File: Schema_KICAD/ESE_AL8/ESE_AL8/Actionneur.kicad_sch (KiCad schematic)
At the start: 15 parts, among them J1 ECRAN, U2 ZXBM5210-SP, U3 ZXBM5210-SP

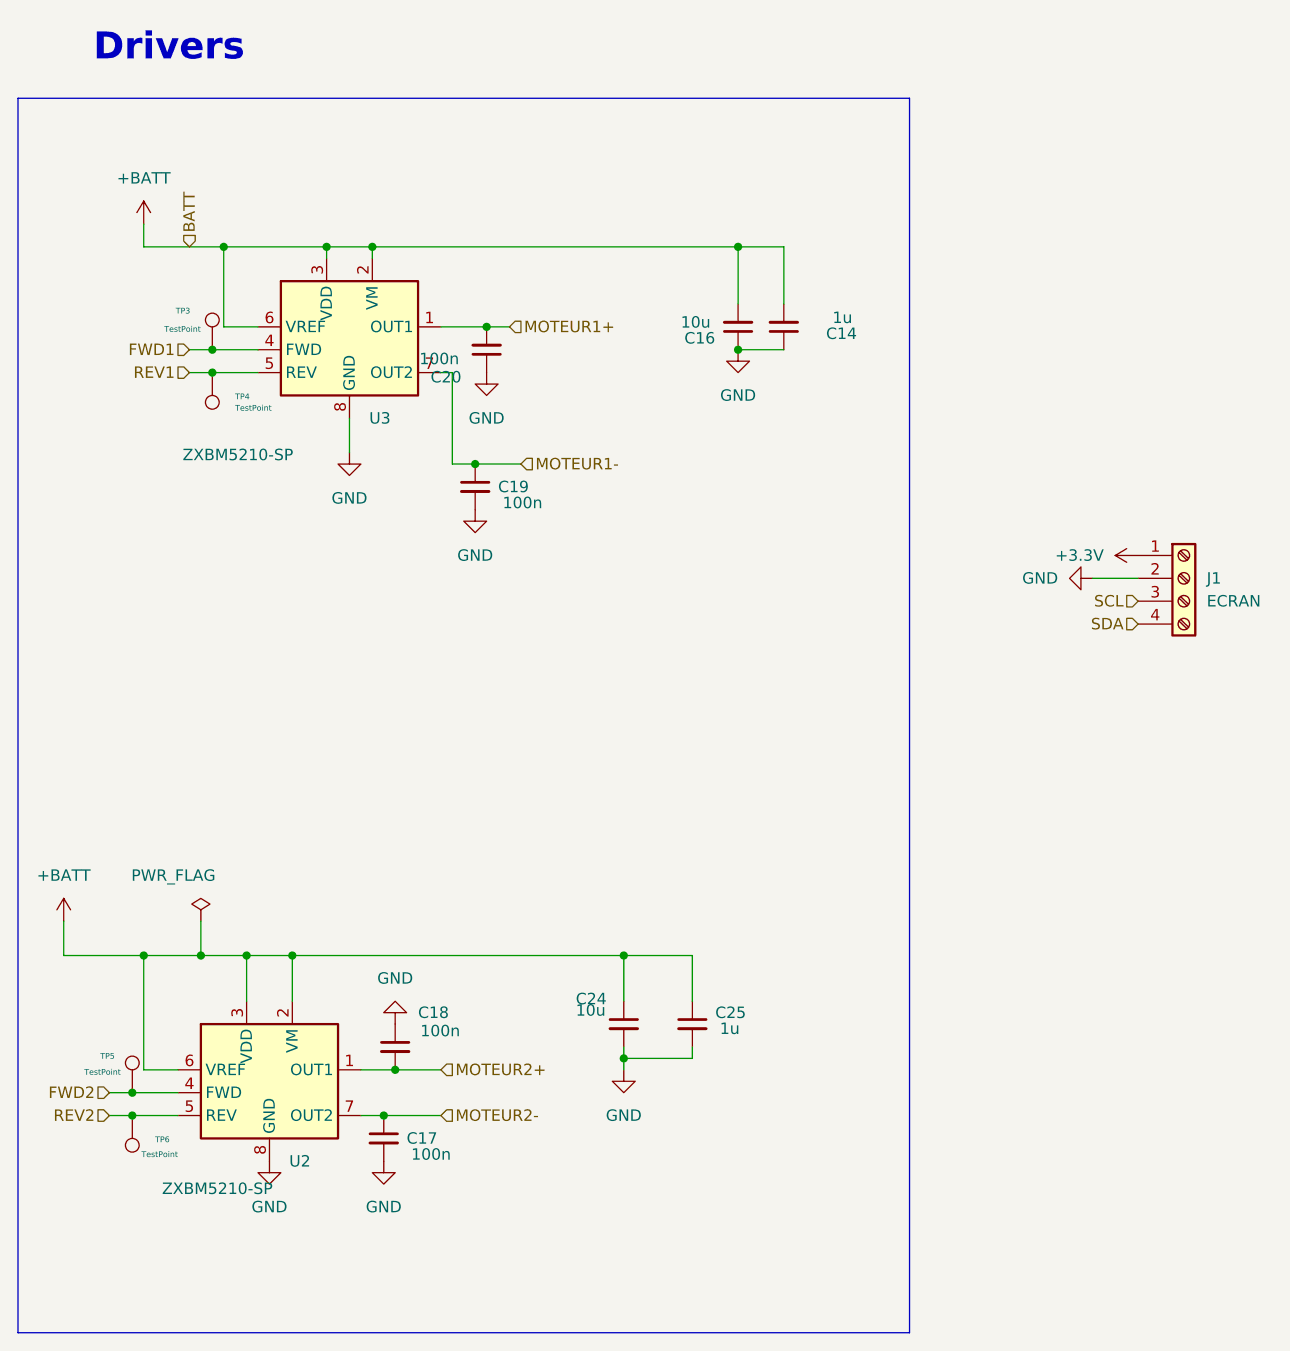
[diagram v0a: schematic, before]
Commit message: Routage aprés correction
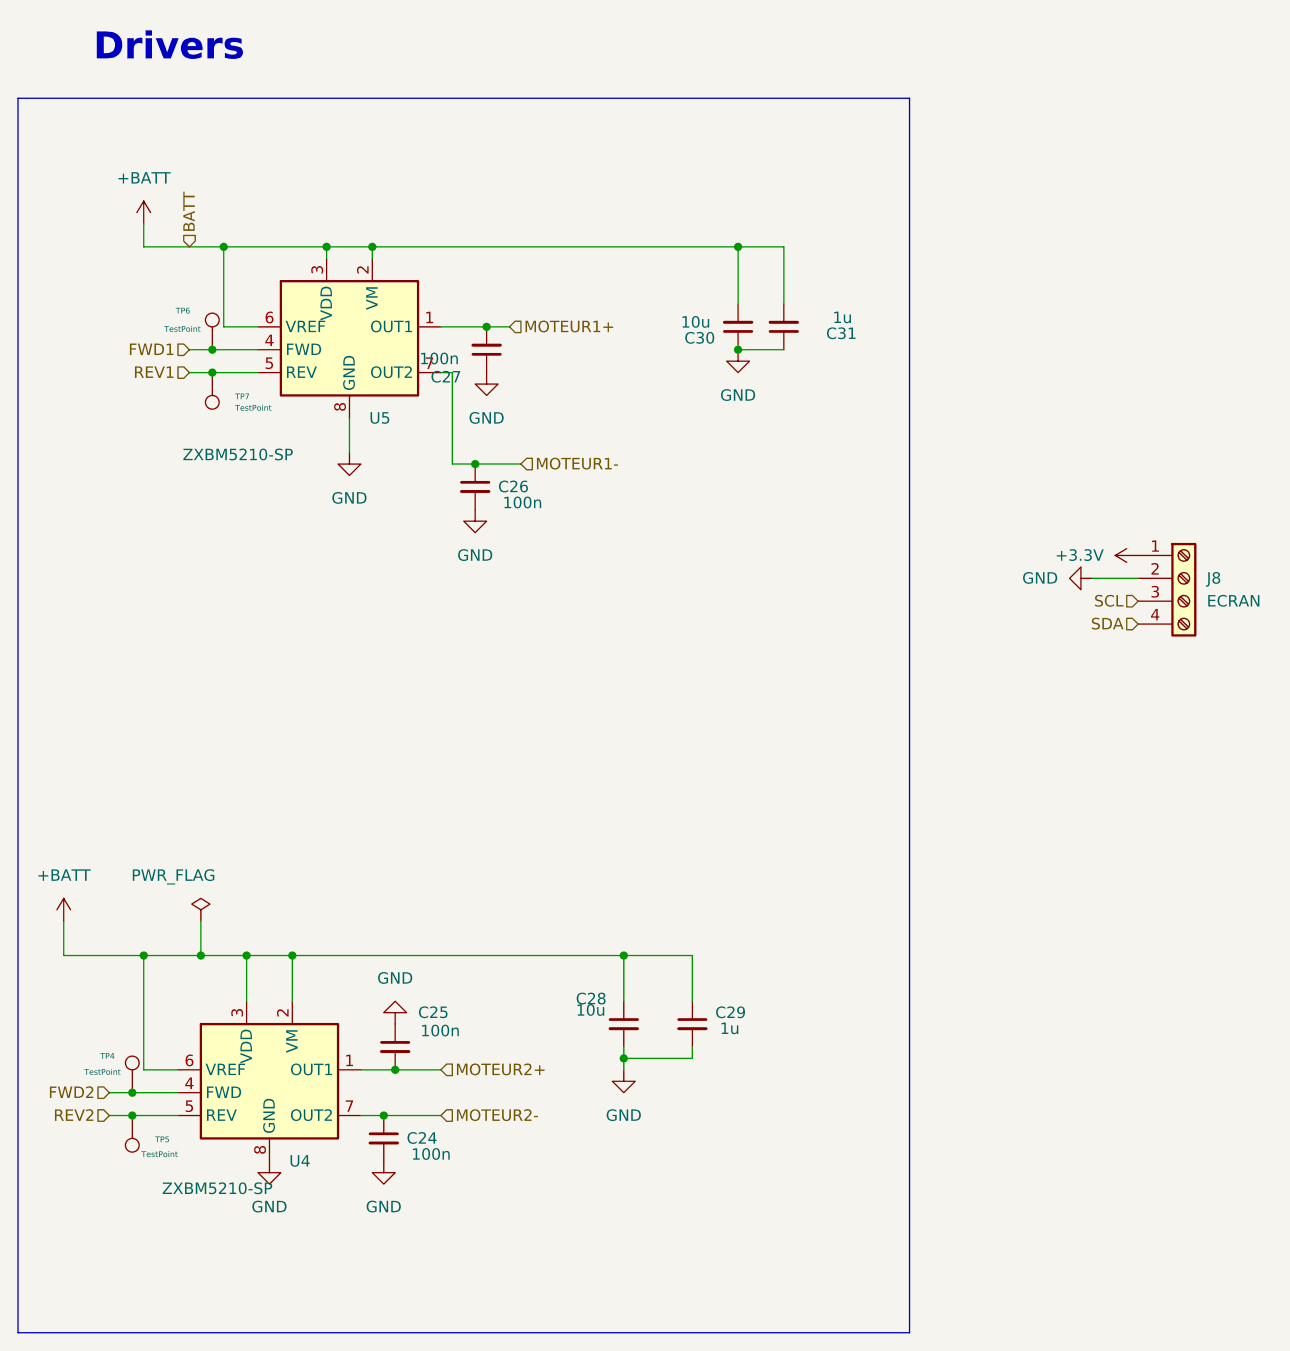
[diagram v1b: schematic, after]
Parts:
- C24: renamed from C17; footprint Capacitor_SMD:C_0402_1005Metric_Pad0.74x0.62mm_HandSolder -> Capacitor_SMD:C_0402_1005Metric
- C25: renamed from C18; footprint Capacitor_SMD:C_0402_1005Metric_Pad0.74x0.62mm_HandSolder -> Capacitor_SMD:C_0402_1005Metric
- C26: renamed from C19; footprint Capacitor_SMD:C_0402_1005Metric_Pad0.74x0.62mm_HandSolder -> Capacitor_SMD:C_0402_1005Metric
- C27: renamed from C20; footprint Capacitor_SMD:C_0402_1005Metric_Pad0.74x0.62mm_HandSolder -> Capacitor_SMD:C_0402_1005Metric
- C28: renamed from C24; footprint Capacitor_SMD:C_0402_1005Metric_Pad0.74x0.62mm_HandSolder -> Capacitor_SMD:C_0603_1608Metric
- C29: renamed from C25; footprint Capacitor_SMD:C_0603_1608Metric_Pad1.08x0.95mm_HandSolder -> Capacitor_SMD:C_0603_1608Metric
- C30: renamed from C16; footprint Capacitor_SMD:C_0603_1608Metric_Pad1.08x0.95mm_HandSolder -> Capacitor_SMD:C_0603_1608Metric
- C31: renamed from C14; footprint Capacitor_SMD:C_0402_1005Metric_Pad0.74x0.62mm_HandSolder -> Capacitor_SMD:C_0603_1608Metric
- J8: renamed from J1; footprint Connector_JST:JST_EH_B4B-EH-A_1x04_P2.50mm_Vertical -> Connector_JST:JST_XH_S4B-XH-A_1x04_P2.50mm_Horizontal
- TP4: renamed from TP5; footprint (none) -> TestPoint:TestPoint_Pad_D1.0mm
- TP5: renamed from TP6; footprint (none) -> TestPoint:TestPoint_Pad_D1.0mm
- TP6: renamed from TP3; footprint (none) -> TestPoint:TestPoint_Pad_D1.0mm
- TP7: renamed from TP4; footprint (none) -> TestPoint:TestPoint_Pad_D1.0mm
- U4: renamed from U2; footprint Package_SO:Diodes_SO-8EP -> STM32:Diodes_SO-8EP
- U5: renamed from U3; footprint Package_SO:Diodes_SO-8EP -> STM32:Diodes_SO-8EP
